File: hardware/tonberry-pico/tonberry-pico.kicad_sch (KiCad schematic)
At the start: 30 parts, among them J1 MicroSD_Breakout, J2 SparkFun I2S Audio Breakout M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, J3 RC522_Breakout, J4 Adafruit_bq25185_5V, J5 UART, J6 WS2812, J7 Buttons, J8 Conn_01x01, Q1 2N7000, Q2 2N7000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

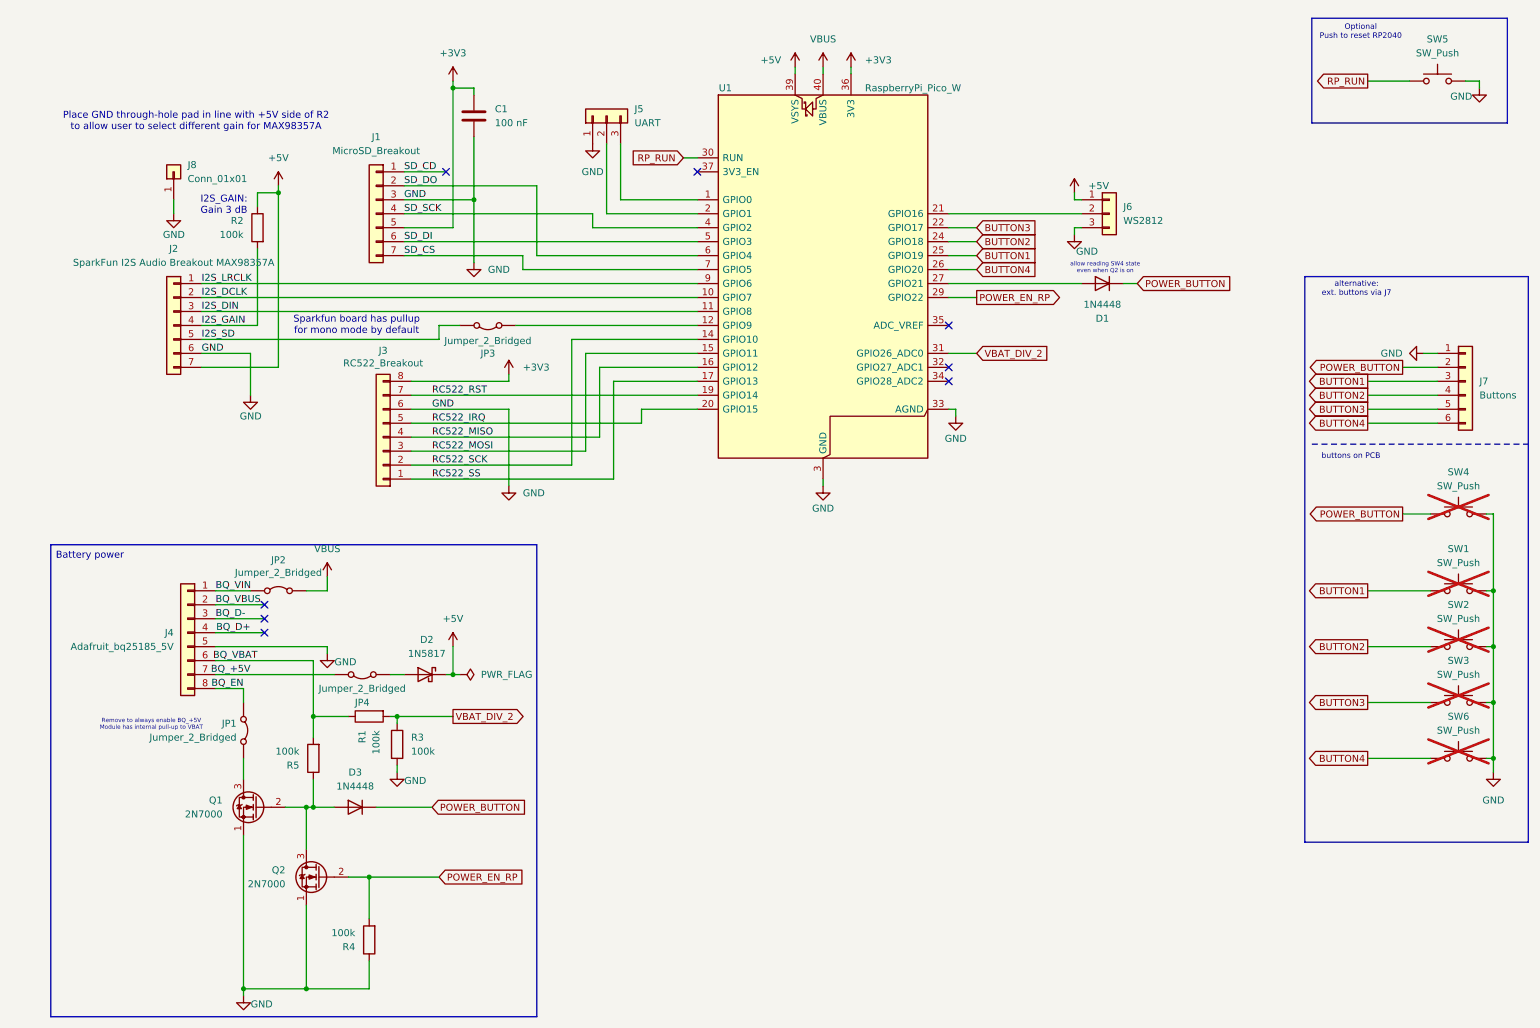
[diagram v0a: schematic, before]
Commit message: hardware: Add MSD-BO1 MicroSD Breakout
The original "SparkFun microSD Transflash Breakout" is not available any
more / currently. Add an additional footprint for the MSD-BO1 MicroSD
Breakout
(https://www.berrybase.de/micro-sd-card-reader-modul-mit-spi-schnittstelle-kompakt)
so that either one can be populated.

The MSD-BO1 has decoupling capacitors on board, so the fact that the
routing of the 3V3 trace does not "go through" the C1 capacitor is
ok. C1 does not need to be populated if the MSD-BO1 is used.

Signed-off-by: Matthias Blankertz <matthias@blankertz.org>
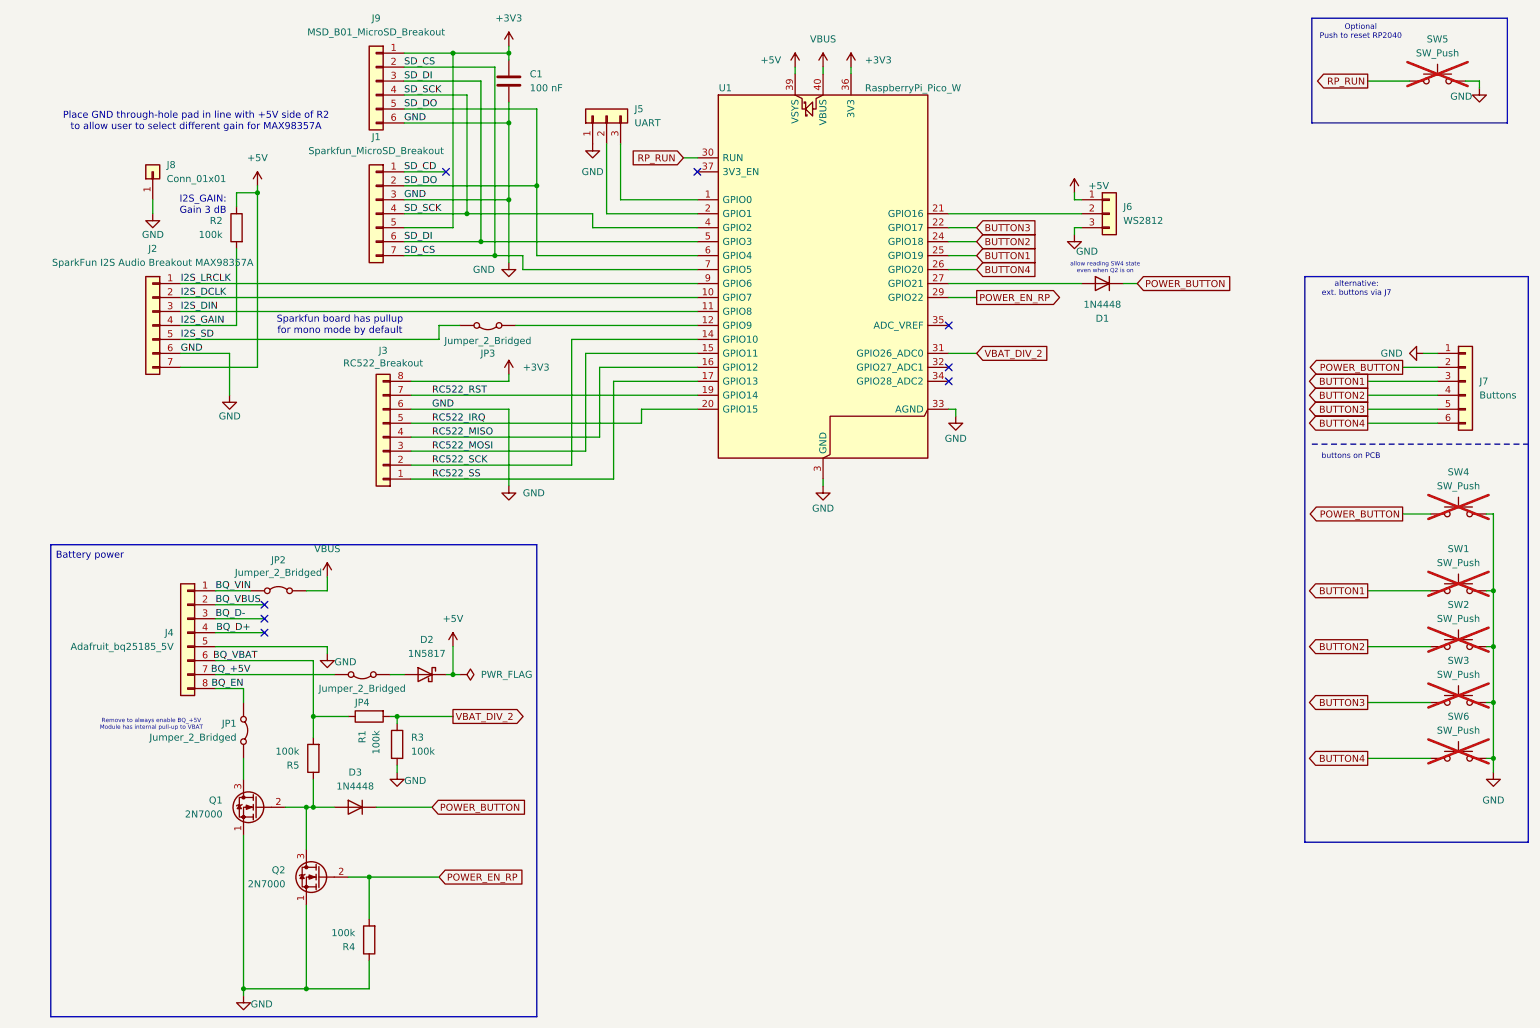
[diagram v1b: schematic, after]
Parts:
- added J9: MSD_B01_MicroSD_Breakout, Modules:MSD_BO1_MicroSD_Breakout_1, symbol Connector_Generic:Conn_01x06
- J1: value MicroSD_Breakout -> Sparkfun_MicroSD_Breakout
- SW5: now not fitted
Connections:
- net +3V3: now also J9.1 (Pin_1)
- net GND: now also J9.6 (Pin_6)
- net SD_CS: now also J9.2 (Pin_2)
- net SD_DI: now also J9.3 (Pin_3)
- net SD_DO: now also J9.5 (Pin_5)
- net SD_SCK: now also J9.4 (Pin_4)
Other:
- moved on the sheet: C1, J2, J8, R2
